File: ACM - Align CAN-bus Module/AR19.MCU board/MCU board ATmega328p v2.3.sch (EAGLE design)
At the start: 37 parts, among them IC1 ATMEGA328P-MMH, IC2 MIC5239-5.0YS_TR, IC3 MCP25625-E_ML, J1 AVR_SPI_PROG_3X2NS

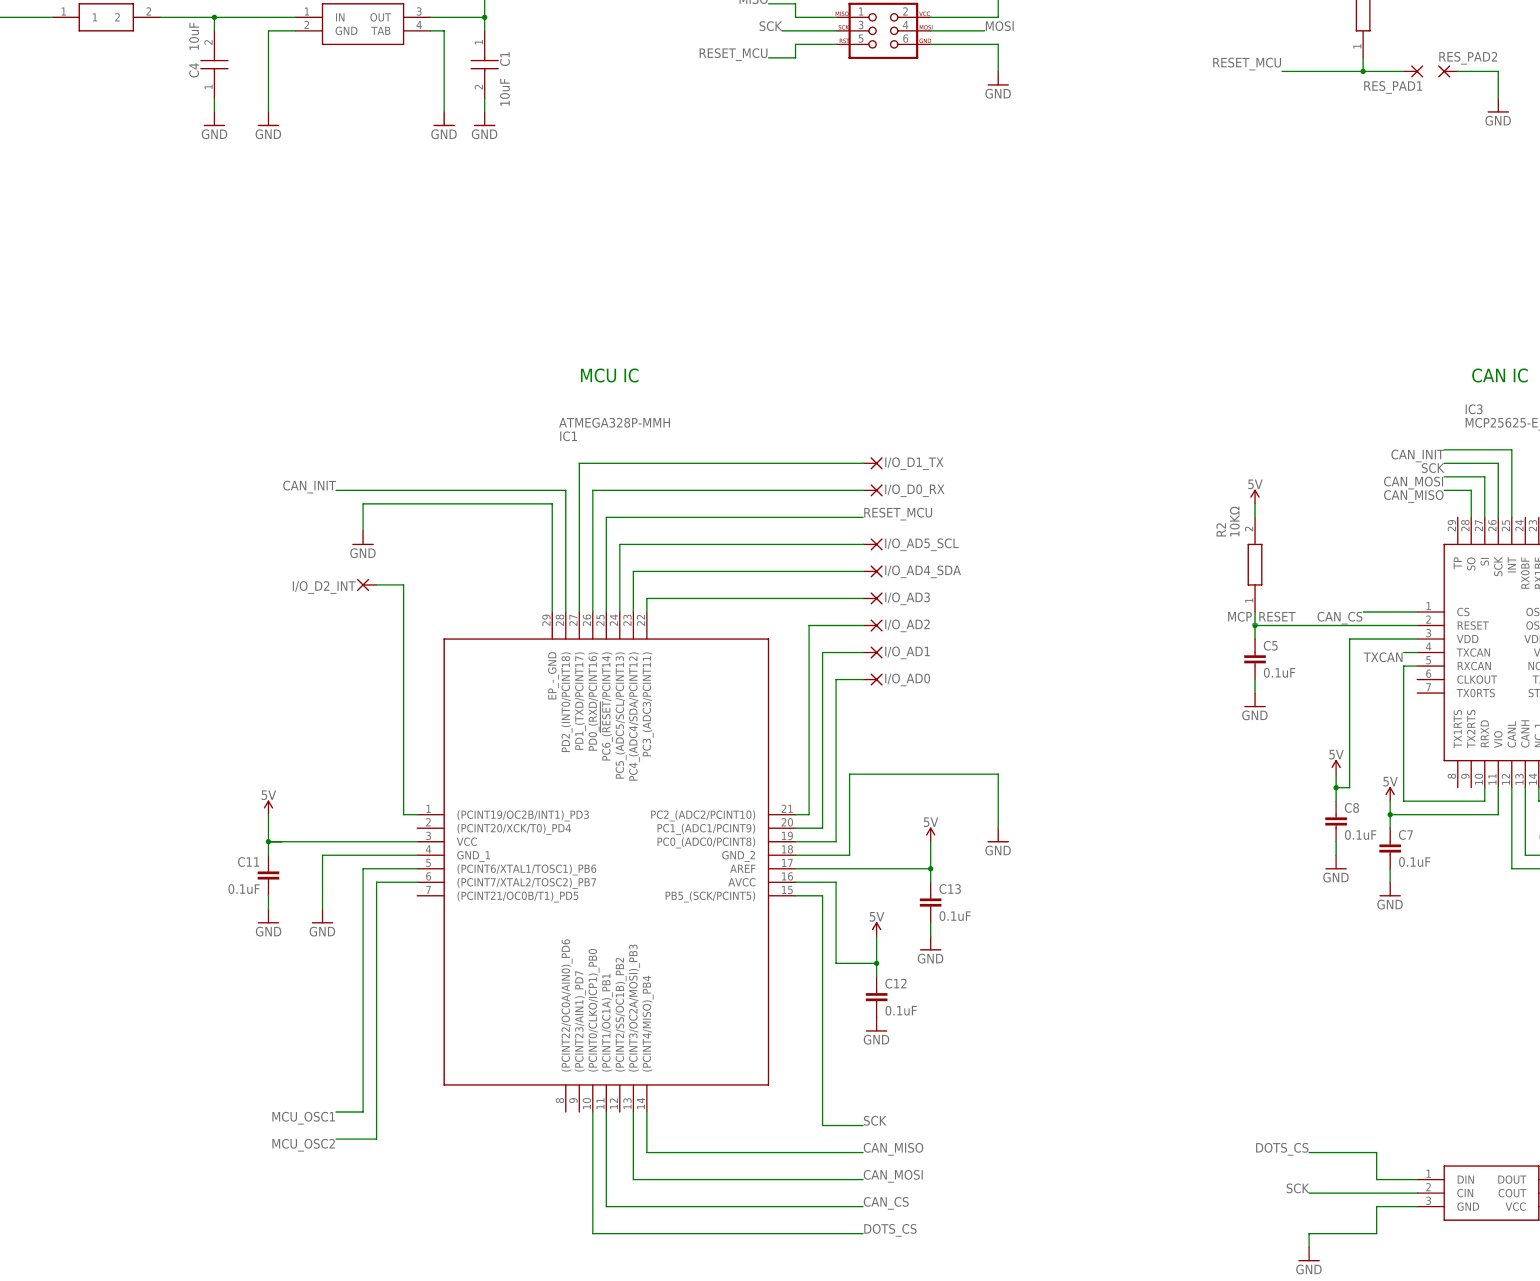
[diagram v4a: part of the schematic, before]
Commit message: Deleted AD0 and minor changes to board file
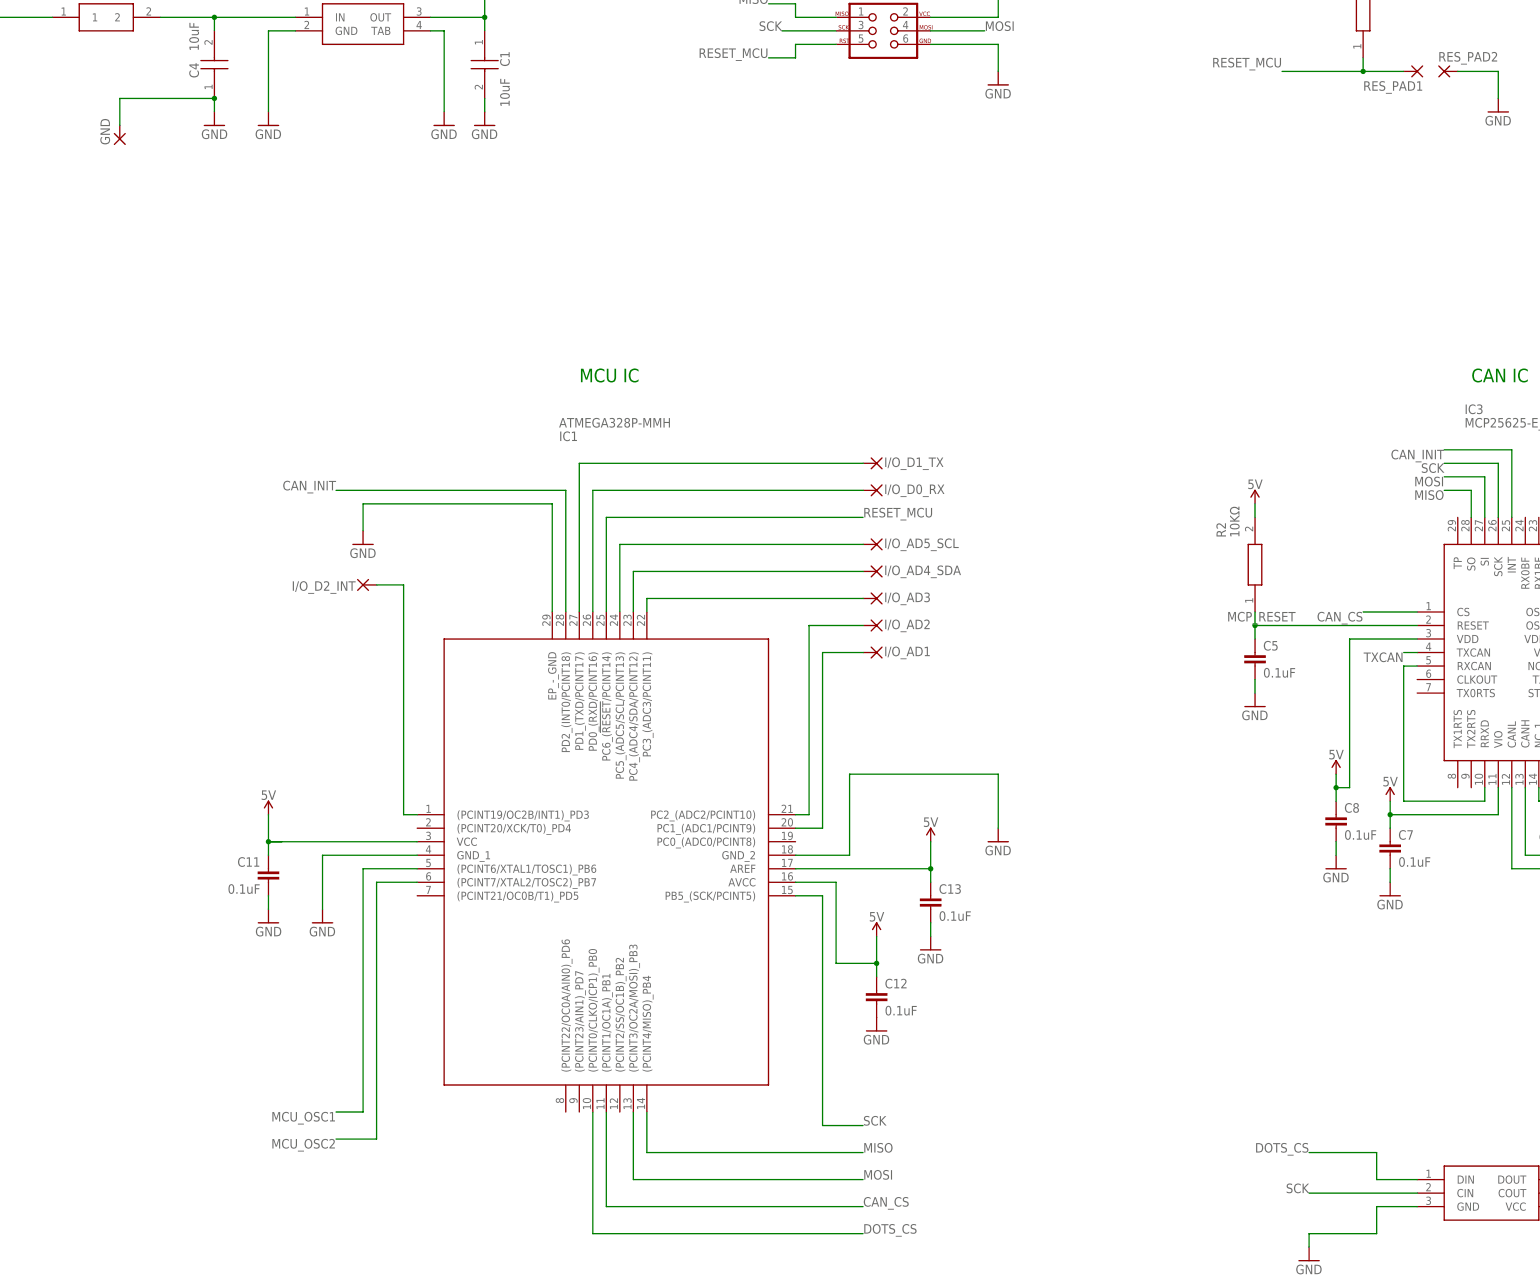
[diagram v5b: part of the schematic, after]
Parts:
- removed I/O_AD0: (no value), wirepad_edit:2,15/1,0(HALFHOLE)H+V
- added GND: (no value), wirepad_edit:2,15/1,0(HALFHOLE)H+V
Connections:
- removed net CAN_MISO: IC1.(PCINT4/MISO)_PB4, IC3.SO
- removed net CAN_MOSI: IC1.(PCINT3/OC2A/MOSI)_PB3, IC3.SI
- removed net I/O_AD0: I/O_AD0.P, IC1.PC0_(ADC0/PCINT8)
- net GND: now also GND.P
- net MISO: now also IC1.(PCINT4/MISO)_PB4, IC3.SO
- net MOSI: now also IC1.(PCINT3/OC2A/MOSI)_PB3, IC3.SI

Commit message: Added: Ratsnest GND on Top and 4th Layer
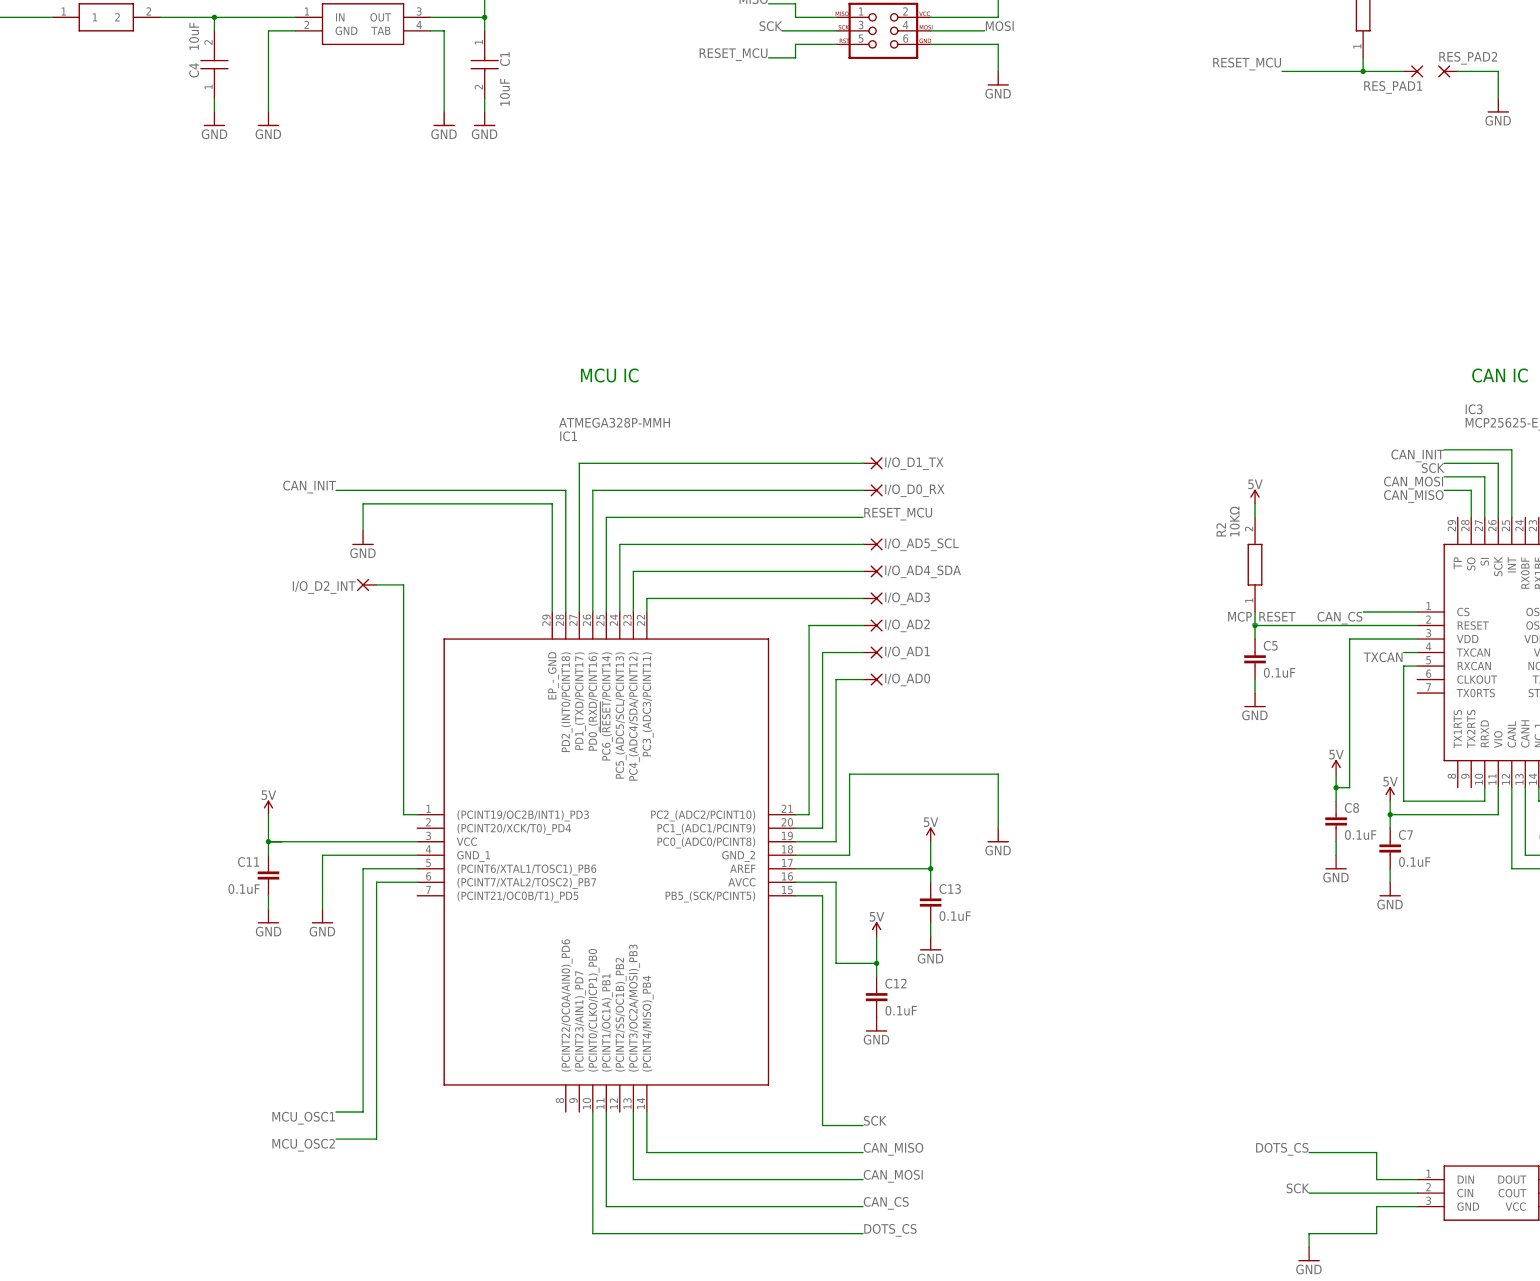
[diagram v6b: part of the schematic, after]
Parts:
- removed GND: (no value), wirepad_edit:2,15/1,0(HALFHOLE)H+V
- added I/O_AD0: (no value), wirepad_edit:2,15/1,0(HALFHOLE)H+V
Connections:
- new net CAN_MISO: IC1.(PCINT4/MISO)_PB4, IC3.SO
- new net CAN_MOSI: IC1.(PCINT3/OC2A/MOSI)_PB3, IC3.SI
- new net I/O_AD0: I/O_AD0.P, IC1.PC0_(ADC0/PCINT8)
- net GND: no longer GND.P
- net MISO: no longer IC1.(PCINT4/MISO)_PB4, IC3.SO
- net MOSI: no longer IC1.(PCINT3/OC2A/MOSI)_PB3, IC3.SI
